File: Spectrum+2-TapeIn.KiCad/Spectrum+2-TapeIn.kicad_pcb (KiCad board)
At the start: 2 copper layers, 40.6 x 27.3 mm, 23 parts, among them U1 LM358

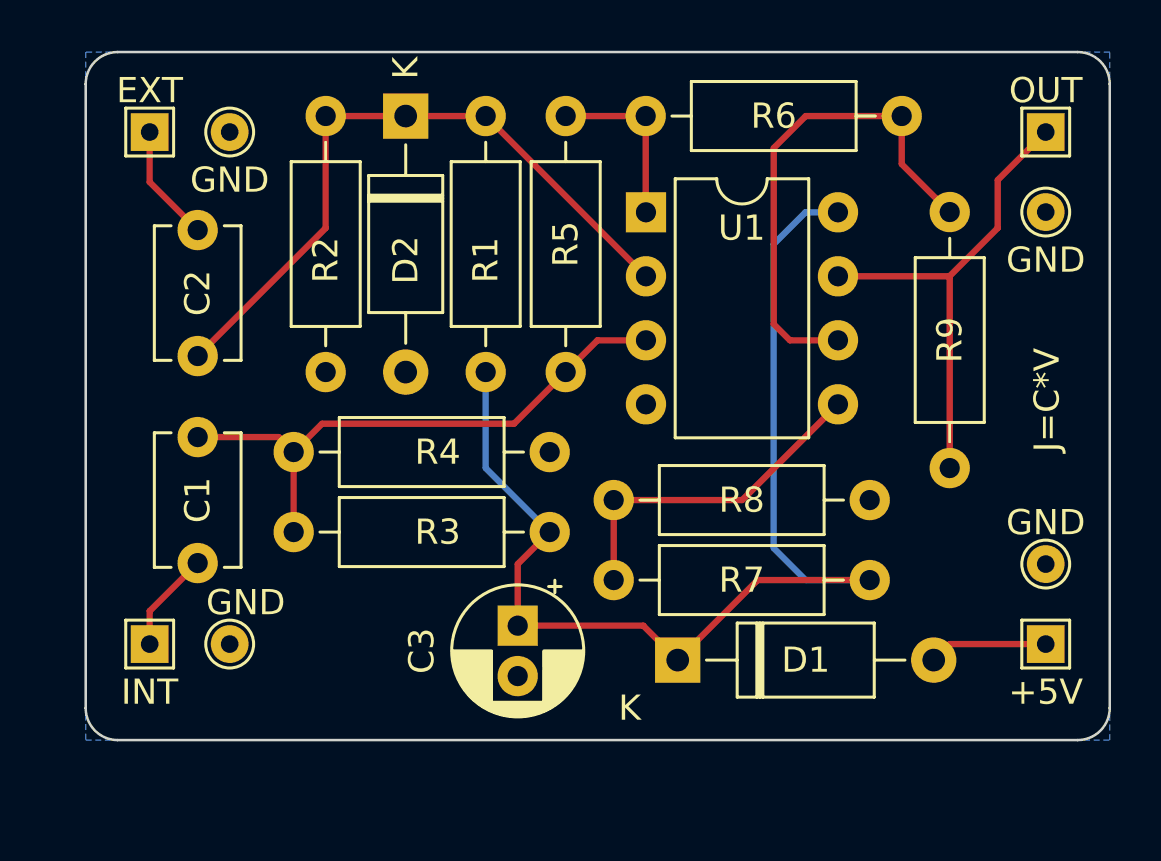
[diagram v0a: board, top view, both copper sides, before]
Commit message: Rev. D
Proper connector for deck plug (no need to cut the wires).
Improved silkscreen, makes it easier to place components when building.
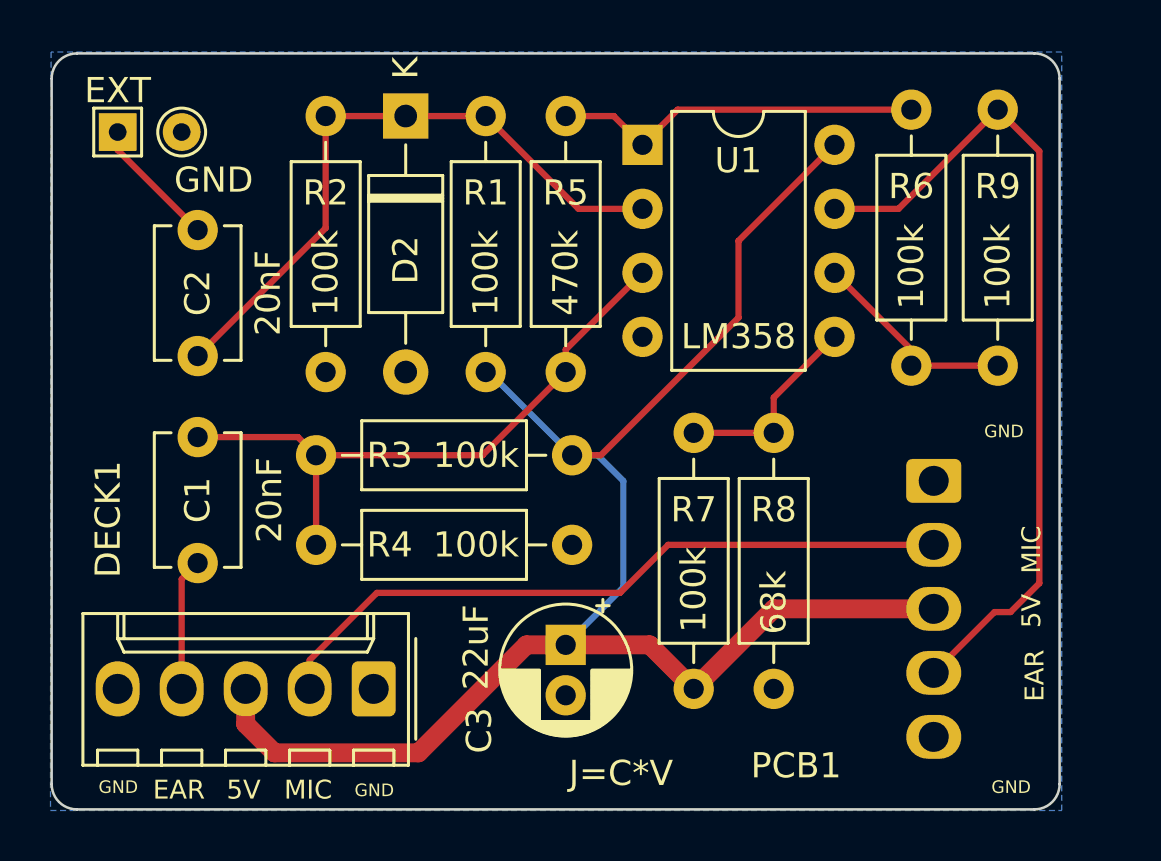
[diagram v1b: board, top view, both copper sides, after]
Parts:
- removed +5V, INT, OUT: TestPoint_THTPad_1.5x1.5mm_Drill0.7mm, TestPoint:TestPoint_THTPad_1.5x1.5mm_Drill0.7mm
- removed D1: ~, Diode_THT:D_A-405_P10.16mm_Horizontal
- removed the GND at (139.1, 91.4)
- removed the GND at (171.4, 88.3)
- removed the GND at (171.4, 74.3)
- added DECK1: Conn_01x05, Connector_Molex:Molex_KK-254_AE-6410-05A_1x05_P2.54mm_Vertical, F.Cu at (144.8, 93.2)
- added PCB1: Conn_01x05, Connector_Molex:Molex_KK-254_AE-6410-05A_1x05_P2.54mm_Vertical, F.Cu at (167.0, 85.0)
- D2: value ~ -> BAT48
- moved R6 10.5 mm to (166.1, 70.2), turned to -90 degrees
- moved R7 8.21 mm to (157.5, 93.2), turned to 90 degrees
- moved R8 6.89 mm to (160.7, 83.1), turned to -90 degrees
- moved R9 6.39 mm to (169.5, 80.4), turned to 90 degrees
- moved R4 3.79 mm to (142.5, 87.5)
- moved R3 3.18 mm to (152.7, 83.9)
- moved U1 2.68 mm to (155.4, 71.6)
- moved C3 2.05 mm to (152.4, 91.5)
- moved GND 1.91 mm to (137.2, 71.1)
- moved EXT 1.27 mm to (134.6, 71.1)
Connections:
- C1 pad 1: INT TAPE -> EAR
- C3 pad 1: +5V -> 5V DC
- R1 pad 1: +5V -> 5V DC
- R3 pad 1: +5V -> 5V DC
- R7 pad 1: +5V -> 5V DC
- U1 pad 8: +5V -> 5V DC
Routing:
- net 5V DC: track 4.71 -> 65.0 mm
- net +5V: track 47.0 -> 0.00 mm
- net MIC: track 0.00 -> 27.8 mm
- net OUTPUT: track 19.3 -> 33.3 mm
- net Net-(U1B--): track 20.0 -> 8.37 mm
- net Net-(R5-Pad2): track 7.65 -> 14.8 mm
- net Net-(U1B-+): track 13.7 -> 7.98 mm
- net EAR: track 0.00 -> 5.26 mm
- net INT TAPE: track 4.00 -> 0.00 mm
- net Net-(U1A-+): track 23.0 -> 25.0 mm
- net Net-(D2-K): track 27.0 -> 25.7 mm
- net EXT TAPE: track 4.68 -> 5.21 mm
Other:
- board size 40.6 x 27.3 mm -> 40 x 30 mm
- board text added: "5V"
- board text added: "EAR"
- board text added: "GND"
- board text added: "MIC"
- board text added: "Rev. ${VCS_REVISION}"
- board text removed: "Rev. C"
